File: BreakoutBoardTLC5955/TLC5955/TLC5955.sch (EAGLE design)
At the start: 3 parts

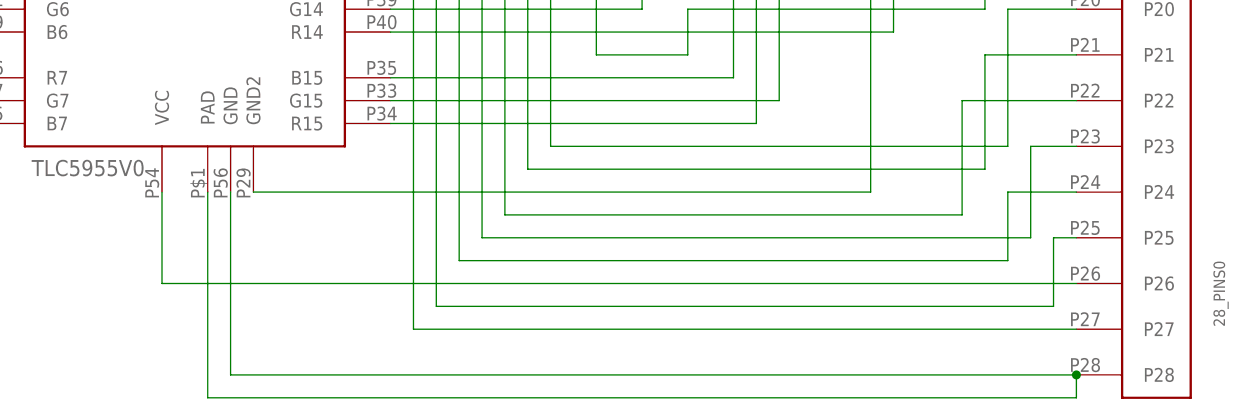
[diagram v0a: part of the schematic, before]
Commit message: TLC Breakout added cap, having trouble with crossed airwires
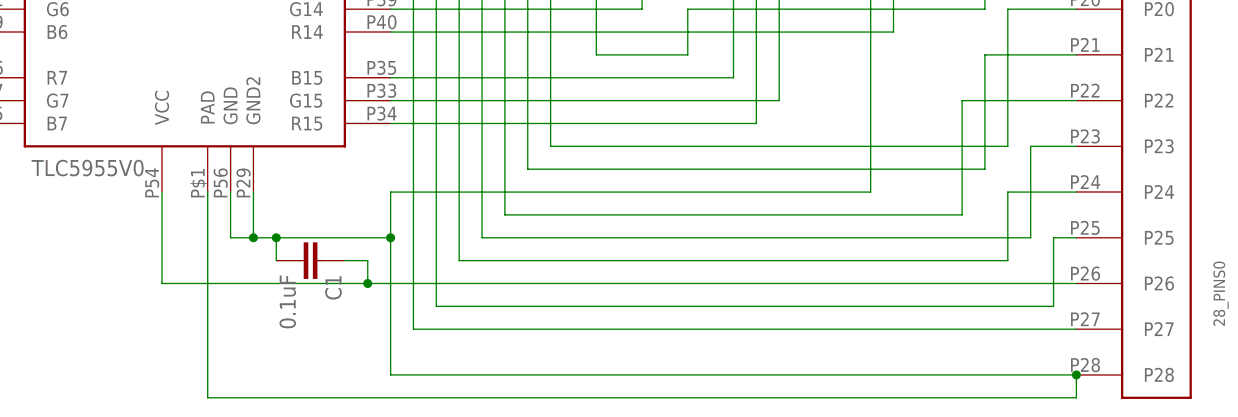
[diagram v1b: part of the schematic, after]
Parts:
- added C1: 0.1uF, SparkFun-Capacitors:0.1UF-25V(+80/-20%)(0603)
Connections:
- removed net N$29: U$1.GND, U$1.PAD, U$3.P28
- removed net N$32: U$1.GND2, U$3.P1
- new net N$57: C1.2, U$1.GND, U$1.GND2, U$1.PAD, U$3.P1, U$3.P28
- net N$31: now also C1.1
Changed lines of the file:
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@@
 <part name="U$2" library="WallerLabLib" deviceset="28_PINS" device="0"/>
 <part name="U$3" library="WallerLabLib" deviceset="28_PINS" device="0"/>
+<part name="C1" library="SparkFun-Capacitors" deviceset="0.1UF-25V(+80/-20%)(0603)" device="" value="0.1uF"/>
 </parts>
 <sheets>
@@
 <instance part="U$2" gate="G$1" x="-22.86" y="68.58" rot="R90"/>
 <instance part="U$3" gate="G$1" x="170.18" y="68.58" rot="R270"/>
+<instance part="C1" gate="G$1" x="76.2" y="12.7" rot="R270"/>
 </instances>
 <busses>
@@
 </segment>
 </net>
-<net name="N$29" class="0">
-<segment>
-<pinref part="U$1" gate="G$1" pin="GND"/>
-<wire x1="68.58" y1="20.32" x2="68.58" y2="0" width="0.1524" layer="91"/>
-<pinref part="U$3" gate="G$1" pin="P28"/>
-<wire x1="68.58" y1="0" x2="162.56" y2="0" width="0.1524" layer="91"/>
-<pinref part="U$1" gate="G$1" pin="PAD"/>
-<wire x1="66.04" y1="20.32" x2="66.04" y2="-2.54" width="0.1524" layer="91"/>
-<wire x1="66.04" y1="-2.54" x2="162.56" y2="-2.54" width="0.1524" layer="91"/>
-<wire x1="162.56" y1="-2.54" x2="162.56" y2="0" width="0.1524" layer="91"/>
-<junction x="162.56" y="0"/>
-</segment>
-</net>
 <net name="N$31" class="0">
 <segment>
@@
 <wire x1="60.96" y1="20.32" x2="60.96" y2="10.16" width="0.1524" layer="91"/>
 <pinref part="U$3" gate="G$1" pin="P26"/>
-<wire x1="60.96" y1="10.16" x2="162.56" y2="10.16" width="0.1524" layer="91"/>
-</segment>
-</net>
-<net name="N$32" class="0">
-<segment>
-<pinref part="U$1" gate="G$1" pin="GND2"/>
-<wire x1="71.12" y1="20.32" x2="139.7" y2="20.32" width="0.1524" layer="91"/>
-<wire x1="139.7" y1="20.32" x2="139.7" y2="137.16" width="0.1524" layer="91"/>
-<pinref part="U$3" gate="G$1" pin="P1"/>
-<wire x1="139.7" y1="137.16" x2="162.56" y2="137.16" width="0.1524" layer="91"/>
+<wire x1="60.96" y1="10.16" x2="83.82" y2="10.16" width="0.1524" layer="91"/>
+<pinref part="C1" gate="G$1" pin="1"/>
+<wire x1="83.82" y1="10.16" x2="162.56" y2="10.16" width="0.1524" layer="91"/>
+<wire x1="81.28" y1="12.7" x2="83.82" y2="12.7" width="0.1524" layer="91"/>
+<wire x1="83.82" y1="12.7" x2="83.82" y2="10.16" width="0.1524" layer="91"/>
+<junction x="83.82" y="10.16"/>
 </segment>
 </net>
@@
 </segment>
 </net>
+<net name="N$57" class="0">
+<segment>
+<pinref part="C1" gate="G$1" pin="2"/>
+<wire x1="73.66" y1="12.7" x2="73.66" y2="15.24" width="0.1524" layer="91"/>
+<pinref part="U$3" gate="G$1" pin="P28"/>
+<wire x1="86.36" y1="0" x2="162.56" y2="0" width="0.1524" layer="91"/>
+<pinref part="U$1" gate="G$1" pin="PAD"/>
+<wire x1="66.04" y1="20.32" x2="66.04" y2="-2.54" width="0.1524" layer="91"/>
+<wire x1="66.04" y1="-2.54" x2="162.56" y2="-2.54" width="0.1524" layer="91"/>
+<wire x1="162.56" y1="-2.54" x2="162.56" y2="0" width="0.1524" layer="91"/>
+<junction x="162.56" y="0"/>
+<wire x1="73.66" y1="15.24" x2="86.36" y2="15.24" width="0.1524" layer="91"/>
+<wire x1="86.36" y1="15.24" x2="86.36" y2="0" width="0.1524" layer="91"/>
+<wire x1="86.36" y1="15.24" x2="86.36" y2="20.32" width="0.1524" layer="91"/>
+<junction x="86.36" y="15.24"/>
+<wire x1="139.7" y1="20.32" x2="139.7" y2="137.16" width="0.1524" layer="91"/>
+<pinref part="U$3" gate="G$1" pin="P1"/>
+<wire x1="139.7" y1="137.16" x2="162.56" y2="137.16" width="0.1524" layer="91"/>
+<wire x1="86.36" y1="20.32" x2="139.7" y2="20.32" width="0.1524" layer="91"/>
+<pinref part="U$1" gate="G$1" pin="GND"/>
+<wire x1="68.58" y1="20.32" x2="68.58" y2="15.24" width="0.1524" layer="91"/>
+<wire x1="68.58" y1="15.24" x2="71.12" y2="15.24" width="0.1524" layer="91"/>
+<junction x="73.66" y="15.24"/>
+<pinref part="U$1" gate="G$1" pin="GND2"/>
+<wire x1="71.12" y1="15.24" x2="73.66" y2="15.24" width="0.1524" layer="91"/>
+<wire x1="71.12" y1="20.32" x2="71.12" y2="15.24" width="0.1524" layer="91"/>
+<junction x="71.12" y="15.24"/>
+</segment>
+</net>

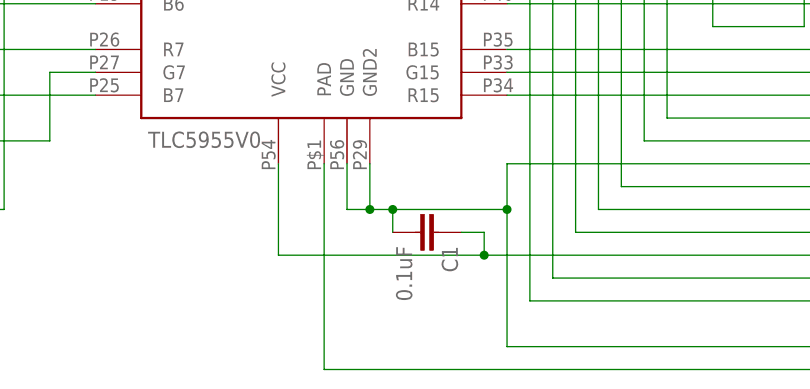
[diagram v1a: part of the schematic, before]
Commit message: Updated TLC board, added .lck files to gitignore
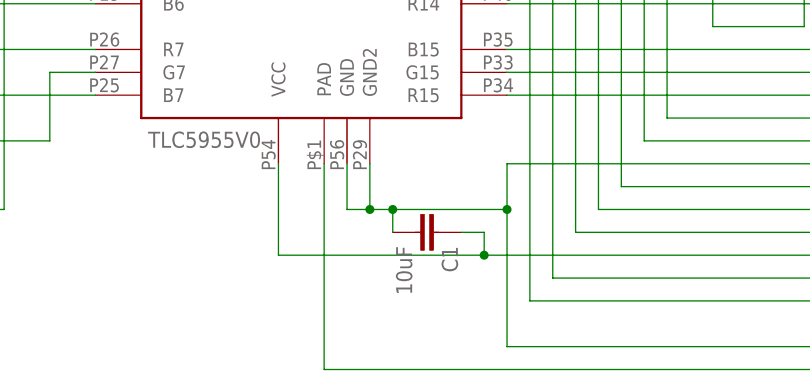
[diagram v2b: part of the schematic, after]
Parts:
- C1: value 0.1uF -> 10uF; device SparkFun-Capacitors:0.1UF-25V(+80/-20%)(0603) -> WallerLabLib:10UF-6.3V-20%(0603)
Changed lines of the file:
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@@
 <?xml version="1.0" encoding="utf-8"?>
 <!DOCTYPE eagle SYSTEM "eagle.dtd">
-<eagle version="7.4.0">
+<eagle version="7.5.0">
 <drawing>
 <settings>
@@
 <part name="U$2" library="WallerLabLib" deviceset="28_PINS" device="0"/>
 <part name="U$3" library="WallerLabLib" deviceset="28_PINS" device="0"/>
-<part name="C1" library="SparkFun-Capacitors" deviceset="0.1UF-25V(+80/-20%)(0603)" device="" value="0.1uF"/>
+<part name="C1" library="WallerLabLib" deviceset="10UF-6.3V-20%(0603)" device="" value="10uF"/>
 </parts>
 <sheets>
